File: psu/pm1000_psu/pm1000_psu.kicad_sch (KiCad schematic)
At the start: 42 parts, among them J1 , J2 , J3 , J4 , J5 , U1 LM317_TO-220, U2 LM317_TO-220, U3 LM317_TO-220

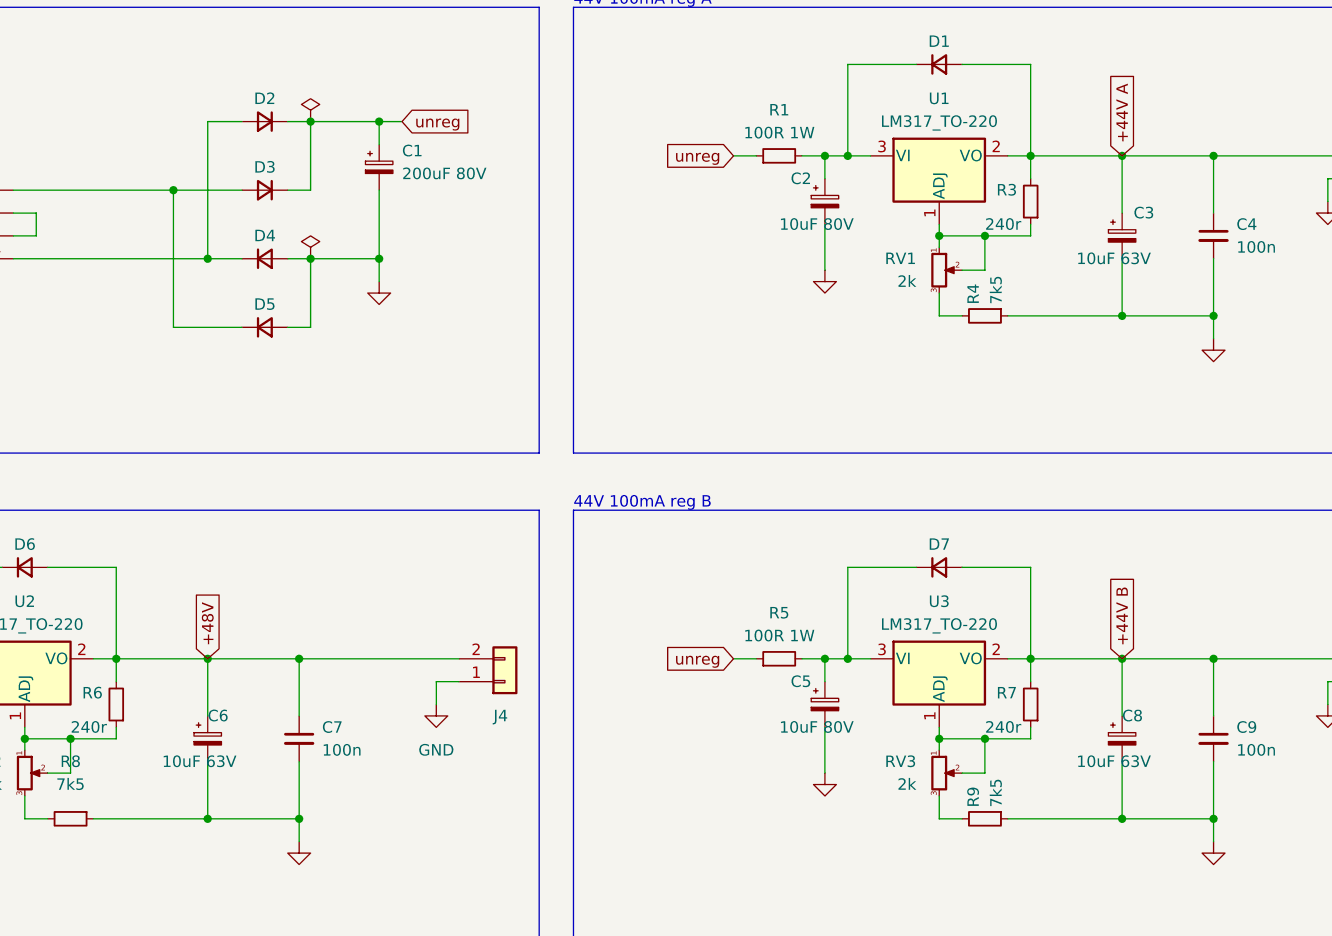
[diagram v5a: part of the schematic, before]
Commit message: update component values and mouser numbers for easy ordering
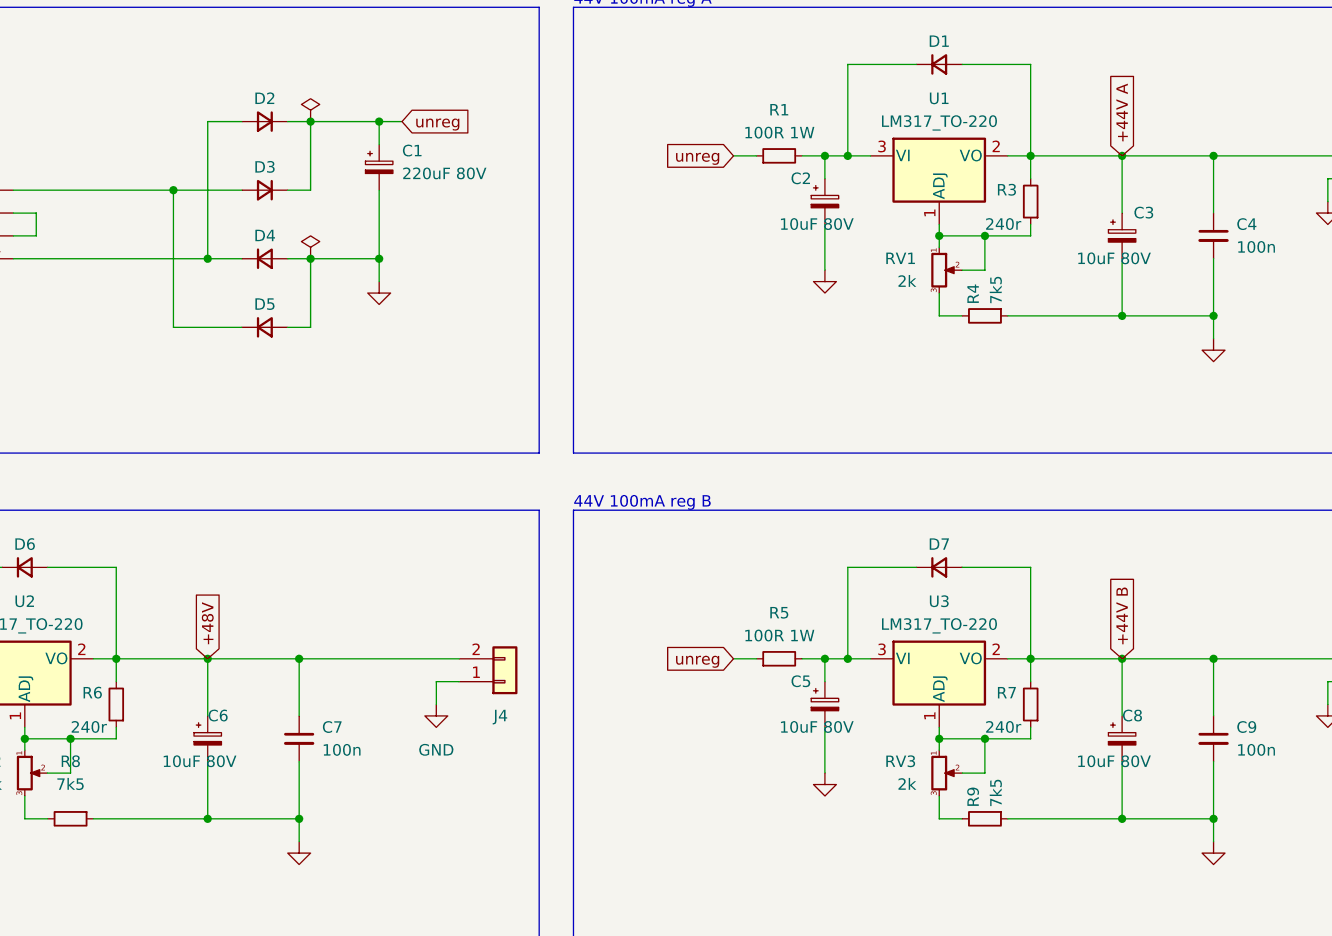
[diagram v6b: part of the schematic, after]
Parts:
- C1: value 200uF 80V -> 220uF 80V; Mouser # (none) -> 667-ECA-2AHG221B
- C2, C5: Mouser # (none) -> 667-ECA-2AM100I
- C3, C6, C8: value 10uF 63V -> 10uF 80V; Mouser # (none) -> 667-ECA-2AM100I
- C4, C7, C9: Mouser # (none) -> 594-K104K15X7RF5TH5
- D1, D2, D3, D4, D5, D6, D7: Mouser # (none) -> 621-1N4007
- D10, D8, D9: Mouser # (none) -> 696-SSL-LX3044HDTR
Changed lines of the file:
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@@
+      (effects (font (size 1.27 1.27)) hide)
+    )
+    (property "Mouser #" " 696-SSL-LX3044HDTR " (id 4) (at 43.18 157.48 0)
       (effects (font (size 1.27 1.27)) hide)
     )
@@
       (effects (font (size 1.27 1.27)) hide)
     )
+    (property "Mouser #" "621-1N4007" (id 4) (at 44.45 83.82 0)
+      (effects (font (size 1.27 1.27)) hide)
+    )
     (pin "1")
     (pin "2")
@@
     )
     (property "Datasheet" "~" (id 3) (at 133.35 43.18 0)
+      (effects (font (size 1.27 1.27)) hide)
+    )
+    (property "Mouser #" "667-ECA-2AM100I " (id 4) (at 133.35 43.18 0)
       (effects (font (size 1.27 1.27)) hide)
     )
@@
       (effects (font (size 1.27 1.27)) hide)
     )
+    (property "Mouser #" "621-1N4007" (id 4) (at 71.12 49.53 0)
+      (effects (font (size 1.27 1.27)) hide)
+    )
     (pin "1")
     (pin "2")
@@
       (effects (font (size 1.27 1.27)) hide)
     )
+    (property "Mouser #" "594-K104K15X7RF5TH5" (id 4) (at 74.93 102.87 0)
+      (effects (font (size 1.27 1.27)) hide)
+    )
     (pin "1")
     (pin "2")
@@
     )
     (property "Datasheet" "~" (id 3) (at 71.12 57.15 90)
+      (effects (font (size 1.27 1.27)) hide)
+    )
+    (property "Mouser #" "621-1N4007" (id 4) (at 71.12 57.15 0)
       (effects (font (size 1.27 1.27)) hide)
     )
@@
       (effects (font (size 1.27 1.27)) hide)
     )
+    (property "Mouser #" "621-1N4007" (id 4) (at 146.05 83.82 0)
+      (effects (font (size 1.27 1.27)) hide)
+    )
     (pin "1")
     (pin "2")
@@
       (effects (font (size 1.27 1.27)) hide)
     )
+    (property "Mouser #" "621-1N4007" (id 4) (at 71.12 41.91 0)
+      (effects (font (size 1.27 1.27)) hide)
+    )
     (pin "1")
     (pin "2")
@@
       (effects (font (size 1.27 1.27)) (justify left))
     )
-    (property "Value" "10uF 63V" (id 1) (at 161.29 105.41 0)
+    (property "Value" "10uF 80V" (id 1) (at 161.29 105.41 0)
       (effects (font (size 1.27 1.27)) (justify left))
     )
@@
       (effects (font (size 1.27 1.27)) hide)
     )
+    (property "Mouser #" "667-ECA-2AM100I " (id 4) (at 166.37 102.87 0)
+      (effects (font (size 1.27 1.27)) hide)
+    )
     (pin "1")
     (pin "2")
@@
       (effects (font (size 1.27 1.27)) (justify left))
     )
-    (property "Value" "200uF 80V" (id 1) (at 86.36 40.0938 0)
+    (property "Value" "220uF 80V" (id 1) (at 86.36 40.0938 0)
       (effects (font (size 1.27 1.27)) (justify left))
     )
@@
     )
     (property "Datasheet" "~" (id 3) (at 83.82 39.37 0)
+      (effects (font (size 1.27 1.27)) hide)
+    )
+    (property "Mouser #" "667-ECA-2AHG221B" (id 4) (at 83.82 39.37 0)
       (effects (font (size 1.27 1.27)) hide)
     )
@@
       (effects (font (size 1.27 1.27)) hide)
     )
+    (property "Mouser #" "621-1N4007" (id 4) (at 146.05 27.94 0)
+      (effects (font (size 1.27 1.27)) hide)
+    )
     (pin "1")
     (pin "2")
@@
       (effects (font (size 1.27 1.27)) hide)
     )
+    (property "Mouser #" "667-ECA-2AM100I " (id 4) (at 133.35 99.06 0)
+      (effects (font (size 1.27 1.27)) hide)
+    )
     (pin "1")
     (pin "2")
@@
     )
     (property "Datasheet" "~" (id 3) (at 176.53 102.87 0)
+      (effects (font (size 1.27 1.27)) hide)
+    )
+    (property "Mouser #" "594-K104K15X7RF5TH5" (id 4) (at 176.53 102.87 0)
       (effects (font (size 1.27 1.27)) hide)
     )
@@
       (effects (font (size 1.27 1.27)) hide)
     )
+    (property "Mouser #" "621-1N4007" (id 4) (at 71.12 34.29 0)
+      (effects (font (size 1.27 1.27)) hide)
+    )
     (pin "1")
     (pin "2")
@@
       (effects (font (size 1.27 1.27)) (justify left))
     )
-    (property "Value" "10uF 63V" (id 1) (at 161.29 49.53 0)
+    (property "Value" "10uF 80V" (id 1) (at 161.29 49.53 0)
       (effects (font (size 1.27 1.27)) (justify left))
     )
@@
       (effects (font (size 1.27 1.27)) hide)
     )
+    (property "Mouser #" "667-ECA-2AM100I " (id 4) (at 166.37 46.99 0)
+      (effects (font (size 1.27 1.27)) hide)
+    )
     (pin "1")
     (pin "2")
@@
       (effects (font (size 1.27 1.27)) hide)
     )
+    (property "Mouser #" " 696-SSL-LX3044HDTR " (id 4) (at 58.42 157.48 0)
+      (effects (font (size 1.27 1.27)) hide)
+    )
     (pin "1")
     (pin "2")
@@
       (effects (font (size 1.27 1.27)) (justify left))
     )
-    (property "Value" "10uF 63V" (id 1) (at 59.69 105.41 0)
+    (property "Value" "10uF 80V" (id 1) (at 59.69 105.41 0)
       (effects (font (size 1.27 1.27)) (justify left))
     )
@@
       (effects (font (size 1.27 1.27)) hide)
     )
+    (property "Mouser #" "667-ECA-2AM100I " (id 4) (at 64.77 102.87 0)
+      (effects (font (size 1.27 1.27)) hide)
+    )
     (pin "1")
     (pin "2")
@@
       (effects (font (size 1.27 1.27)) hide)
     )
+    (property "Mouser #" " 696-SSL-LX3044HDTR " (id 4) (at 73.66 157.48 0)
+      (effects (font (size 1.27 1.27)) hide)
+    )
     (pin "1")
     (pin "2")
@@
     )
     (property "Datasheet" "~" (id 3) (at 176.53 46.99 0)
+      (effects (font (size 1.27 1.27)) hide)
+    )
+    (property "Mouser #" "594-K104K15X7RF5TH5" (id 4) (at 176.53 46.99 0)
       (effects (font (size 1.27 1.27)) hide)
     )
@@
     )
     (path "/727e8733-7cce-4712-b3bb-54ee7506b9cf"
-      (reference "C1") (unit 1) (value "200uF 80V") (footprint "Capacitor_THT:CP_Radial_D12.5mm_P5.00mm")
+      (reference "C1") (unit 1) (value "220uF 80V") (footprint "Capacitor_THT:CP_Radial_D12.5mm_P5.00mm")
     )
     (path "/2afdca86-4706-43cb-9dd3-a466883f2b0b"
@@
     )
     (path "/d1c2533e-8916-49fb-93cd-e1fa0e3875cb"
-      (reference "C3") (unit 1) (value "10uF 63V") (footprint "Capacitor_THT:CP_Radial_D6.3mm_P2.50mm")
+      (reference "C3") (unit 1) (value "10uF 80V") (footprint "Capacitor_THT:CP_Radial_D6.3mm_P2.50mm")
     )
     (path "/e3cefe3b-3a3e-4c0a-8c4e-a44cf2518b50"
@@
     )
     (path "/d6eb1862-8b77-426f-a36e-e5267203672e"
-      (reference "C6") (unit 1) (value "10uF 63V") (footprint "Capacitor_THT:CP_Radial_D6.3mm_P2.50mm")
+      (reference "C6") (unit 1) (value "10uF 80V") (footprint "Capacitor_THT:CP_Radial_D6.3mm_P2.50mm")
     )
     (path "/4daa3927-cb01-49a5-b3b7-059e872fca60"
@@
     )
     (path "/706f1f67-342f-453e-a569-e5472b8f97dc"
-      (reference "C8") (unit 1) (value "10uF 63V") (footprint "Capacitor_THT:CP_Radial_D6.3mm_P2.50mm")
+      (reference "C8") (unit 1) (value "10uF 80V") (footprint "Capacitor_THT:CP_Radial_D6.3mm_P2.50mm")
     )
     (path "/9e9edf5d-be2b-4058-a133-7de13765c987"

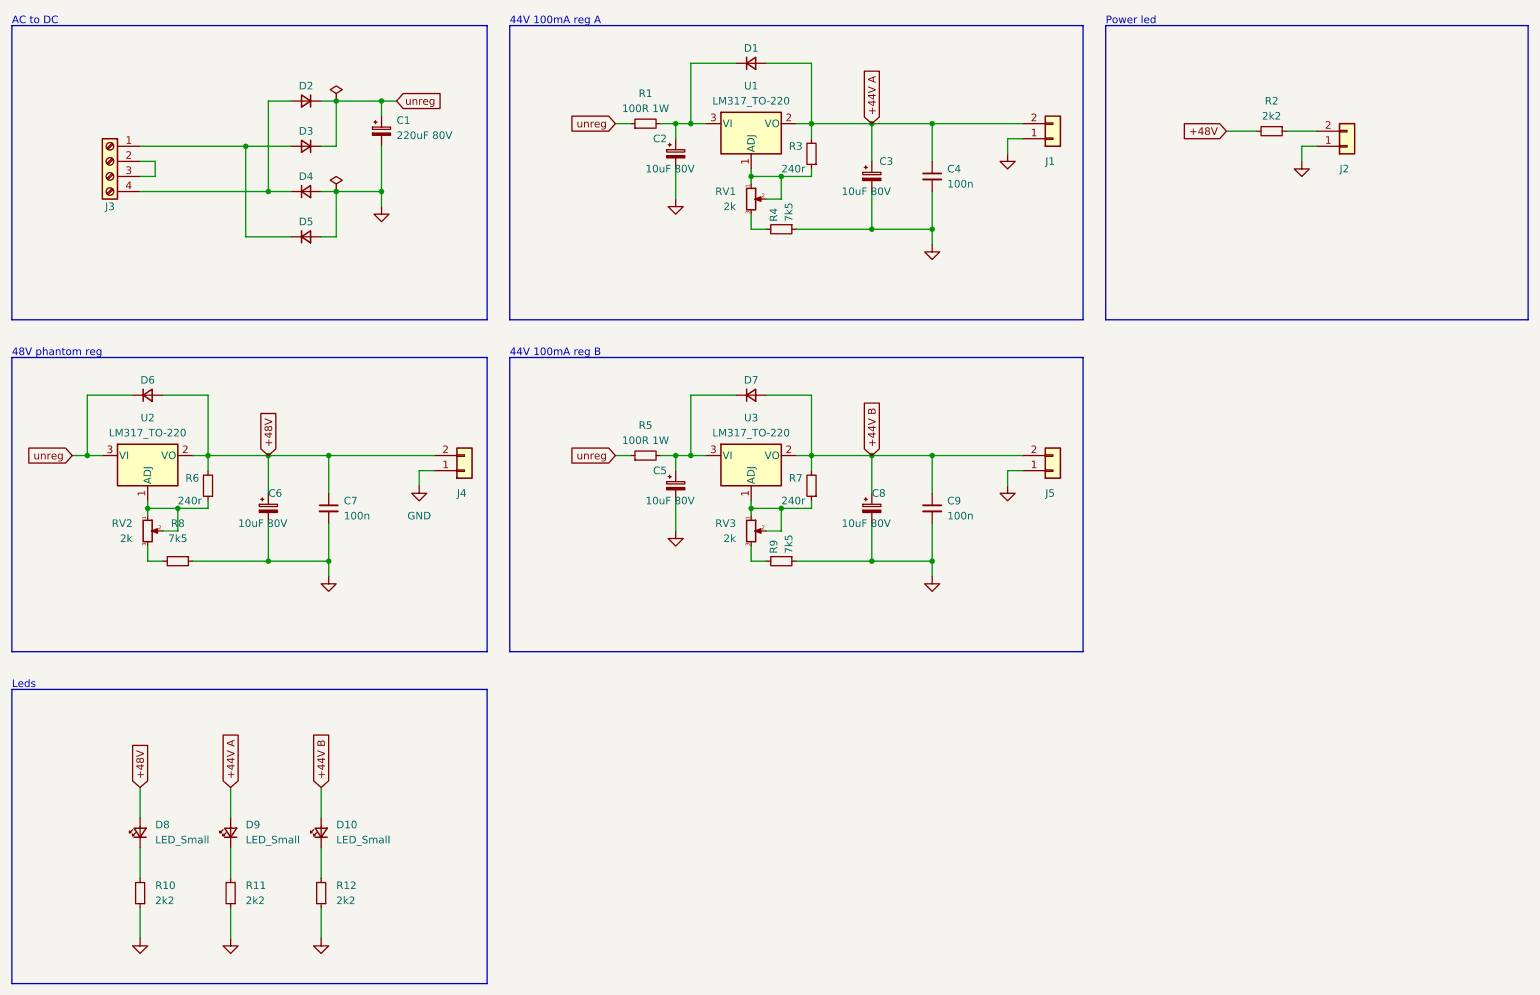
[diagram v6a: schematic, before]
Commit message: clean up projects and update to kicad 9
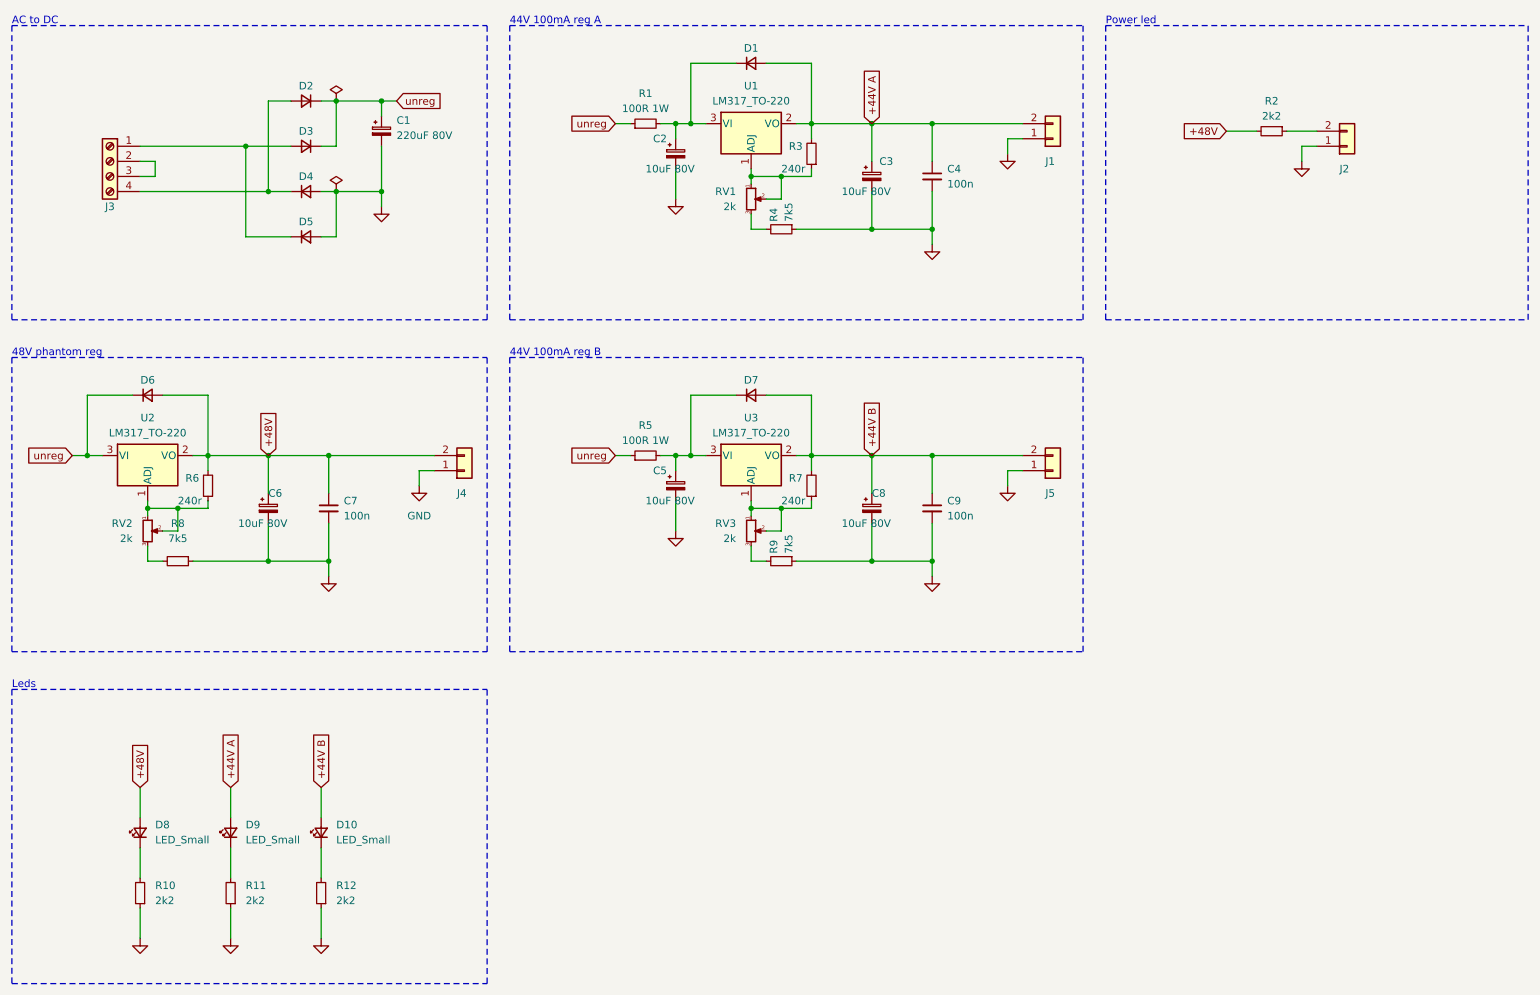
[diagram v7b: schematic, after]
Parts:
- J1, J2, J3, J4, J5: value (none) -> (none)
